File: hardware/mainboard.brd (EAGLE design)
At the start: 160 x 100 mm, 88 parts, among them IC1 ATMEGA328, IC10 HM628512A_DIL32, IC11 HM628512A_DIL32, IC12 7805TV, IC13 DS1210-8PDIP, IC14 6N138, IC3 TLC074, IC4 74HCT04N, IC5 74HC238N, IC6 74HCT573N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

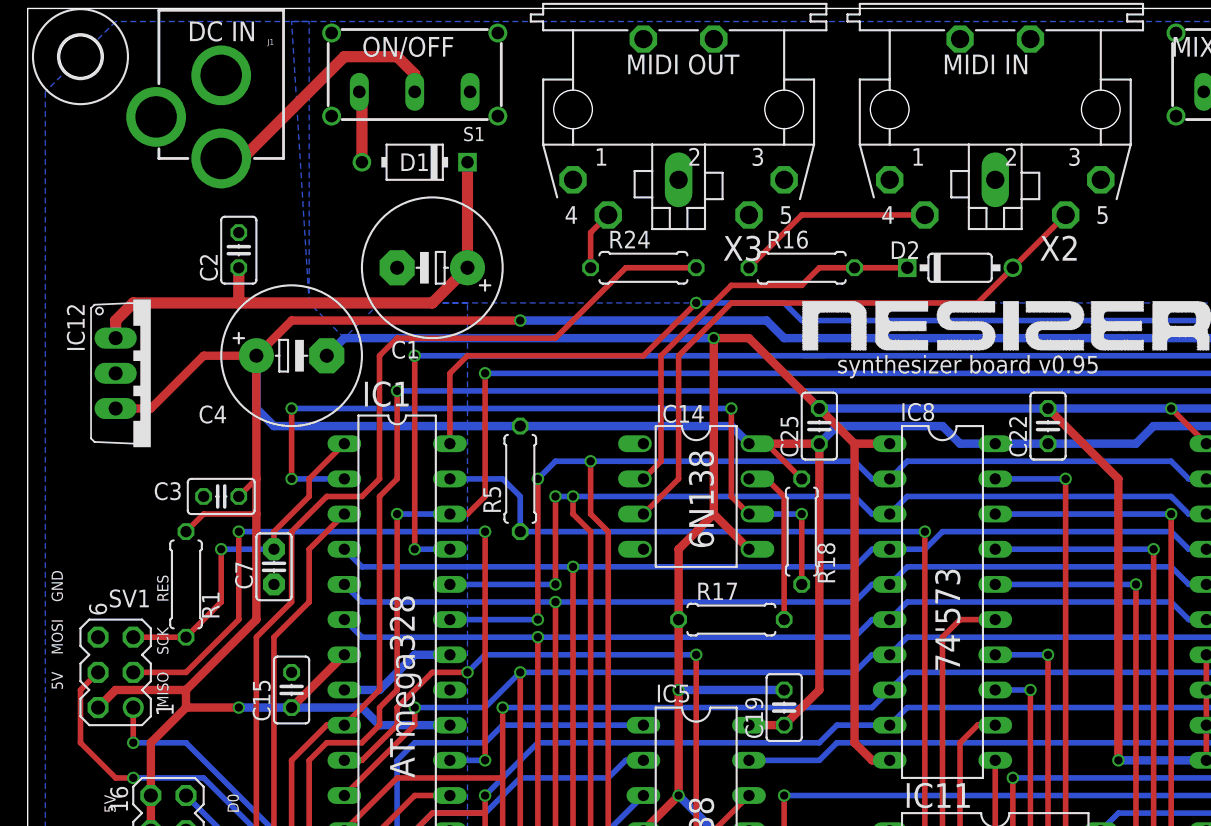
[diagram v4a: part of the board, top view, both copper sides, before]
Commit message: add 220 resistor to MIDI out
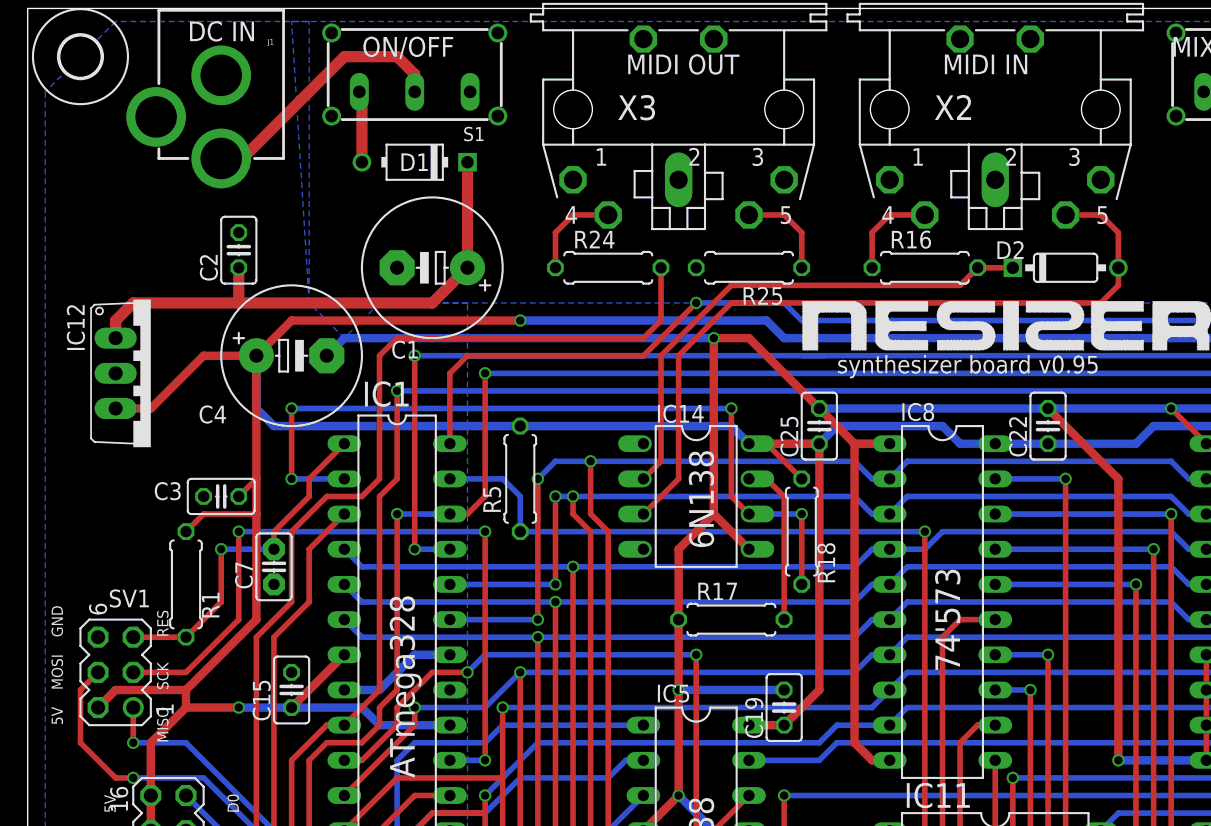
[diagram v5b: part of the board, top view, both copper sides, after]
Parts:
- added R25: 220, rcl:0207/7
- moved R16 8.89 mm to (64.8, 81.3)
- moved D2 7.62 mm to (74.9, 81.3)
- moved R24 2.54 mm to (41.9, 81.3)
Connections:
- new net N$42: R25.1, X3.5
- net GND: now also R25.2; no longer X3.5
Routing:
- net MIDI_PIN_5: track 44.6 -> 54.5 mm
- net N$34: track 29.8 -> 37.4 mm
- net MIDI_PIN_4: track 14.3 -> 6.88 mm
- net N$42: track 0.00 -> 6.88 mm
- net N$41: track 4.34 -> 6.88 mm
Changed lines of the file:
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@@
 <text x="3.81" y="26.67" size="0.8128" layer="25" font="vector" rot="R90">FRONT PANEL CONNECTOR</text>
 <text x="142.24" y="96.52" size="1.4224" layer="25" font="vector">VOLUME</text>
-<text x="2.54" y="50.8" size="0.8128" layer="25" font="vector" rot="R90">5V</text>
-<text x="2.54" y="57.15" size="0.8128" layer="25" font="vector" rot="R90">GND</text>
-<text x="2.54" y="53.34" size="0.8128" layer="25" font="vector" rot="R90">MOSI</text>
-<text x="10.16" y="49.53" size="0.8128" layer="25" font="vector" rot="R90">MISO</text>
-<text x="10.16" y="53.34" size="0.8128" layer="25" font="vector" rot="R90">SCK</text>
-<text x="10.16" y="57.15" size="0.8128" layer="25" font="vector" rot="R90">RES</text>
+<text x="2.54" y="48.26" size="0.8128" layer="25" font="vector" rot="R90">5V</text>
+<text x="2.54" y="54.61" size="0.8128" layer="25" font="vector" rot="R90">GND</text>
+<text x="2.54" y="50.8" size="0.8128" layer="25" font="vector" rot="R90">MOSI</text>
+<text x="10.16" y="46.99" size="0.8128" layer="25" font="vector" rot="R90">MISO</text>
+<text x="10.16" y="50.8" size="0.8128" layer="25" font="vector" rot="R90">SCK</text>
+<text x="10.16" y="54.61" size="0.8128" layer="25" font="vector" rot="R90">RES</text>
 <text x="71.12" y="12.7" size="1.778" layer="21" rot="R90">SRAM 512kx8</text>
 <text x="92.71" y="12.7" size="1.778" layer="21" rot="R90">SRAM 512kx8</text>
@@
 <attribute name="OC_FARNELL" value="9860150" x="48.26" y="64.77" size="1.778" layer="27" rot="R270" display="off"/>
 </element>
-<element name="R16" library="rcl" package="0207/7" value="220" x="55.88" y="81.28"/>
-<element name="D2" library="gm-diodes" package="DO35-3" value="1N914.3" x="67.31" y="81.28" smashed="yes">
-<attribute name="NAME" x="62.23" y="81.915" size="1.27" layer="25" ratio="12"/>
-<attribute name="VALUE" x="65.024" y="78.613" size="1.27" layer="27" ratio="12"/>
+<element name="R16" library="rcl" package="0207/7" value="220" x="64.77" y="81.28"/>
+<element name="D2" library="gm-diodes" package="DO35-3" value="1N914.3" x="74.93" y="81.28" smashed="yes">
+<attribute name="NAME" x="69.85" y="81.915" size="1.27" layer="25" ratio="12"/>
+<attribute name="VALUE" x="72.644" y="78.613" size="1.27" layer="27" ratio="12"/>
 </element>
 <element name="R18" library="rcl" package="0207/7" value="220" x="55.88" y="62.23" smashed="yes" rot="R90">
@@
 <attribute name="VALUE" x="143.891" y="45.974" size="1.27" layer="27" ratio="10" rot="R180"/>
 </element>
-<element name="X2" library="con-hirschmann" package="MAB5SH" value="MAB5SH" x="69.85" y="92.71" rot="R180">
+<element name="X2" library="con-hirschmann" package="MAB5SH" value="MAB5SH" x="69.85" y="92.71" smashed="yes" rot="R180">
 <attribute name="MPN" value="" x="69.85" y="92.71" size="1.778" layer="27" rot="R180" display="off"/>
 <attribute name="OC_NEWARK" value="unknown" x="69.85" y="92.71" size="1.778" layer="27" rot="R180" display="off"/>
 <attribute name="OC_FARNELL" value="809883" x="69.85" y="92.71" size="1.778" layer="27" rot="R180" display="off"/>
 <attribute name="MF" value="" x="69.85" y="92.71" size="1.778" layer="27" rot="R180" display="off"/>
+<attribute name="NAME" x="68.326" y="93.726" size="1.778" layer="25" ratio="10" rot="R180"/>
+<attribute name="VALUE" x="74.93" y="92.71" size="1.778" layer="27" ratio="10" rot="R180"/>
 </element>
 <element name="IC13" library="maxim-custom" package="DIL08" value="DS1210-8PDIP" x="121.92" y="6.35" rot="R270"/>
@@
 </element>
 <element name="C7" library="capacitor-wima" package="C2.5-2" value="10n" x="17.78" y="59.69" rot="R90"/>
-<element name="X3" library="con-hirschmann" package="MAB5SH" value="MAB5SH" x="46.99" y="92.71" rot="R180">
+<element name="X3" library="con-hirschmann" package="MAB5SH" value="MAB5SH" x="46.99" y="92.71" smashed="yes" rot="R180">
 <attribute name="OC_NEWARK" value="unknown" x="46.99" y="92.71" size="1.778" layer="27" rot="R180" display="off"/>
 <attribute name="MF" value="" x="46.99" y="92.71" size="1.778" layer="27" rot="R180" display="off"/>
 <attribute name="MPN" value="" x="46.99" y="92.71" size="1.778" layer="27" rot="R180" display="off"/>
 <attribute name="OC_FARNELL" value="809883" x="46.99" y="92.71" size="1.778" layer="27" rot="R180" display="off"/>
-</element>
-<element name="R24" library="rcl" package="0207/7" value="220" x="44.45" y="81.28"/>
+<attribute name="NAME" x="45.466" y="93.726" size="1.778" layer="25" ratio="10" rot="R180"/>
+<attribute name="VALUE" x="52.07" y="92.71" size="1.778" layer="27" ratio="10" rot="R180"/>
+</element>
+<element name="R24" library="rcl" package="0207/7" value="220" x="41.91" y="81.28"/>
+<element name="R25" library="rcl" package="0207/7" value="220" x="52.07" y="81.28" rot="R180"/>
 </elements>
 <signals>
@@
 <contactref element="C7" pad="1"/>
 <contactref element="X3" pad="2"/>
-<contactref element="X3" pad="5"/>
 <contactref element="X3" pad="PE@"/>
 <contactref element="X3" pad="PE"/>
+<contactref element="R25" pad="2"/>
 </signal>
 <signal name="VCC">
@@
 <signal name="MIDI_PIN_4">
 <contactref element="R16" pad="1"/>
-<wire x1="52.07" y1="81.28" x2="55.88" y2="85.09" width="0.4064" layer="1"/>
 <contactref element="X2" pad="4"/>
-<wire x1="64.77" y1="85.09" x2="55.88" y2="85.09" width="0.4064" layer="1"/>
+<wire x1="60.96" y1="81.28" x2="60.96" y2="83.82" width="0.4064" layer="1"/>
+<wire x1="60.96" y1="83.82" x2="62.23" y2="85.09" width="0.4064" layer="1"/>
+<wire x1="62.23" y1="85.09" x2="64.77" y2="85.09" width="0.4064" layer="1"/>
 </signal>
 <signal name="MIDI_PIN_5">
@@
 <contactref element="D2" pad="A"/>
 <wire x1="44.45" y1="63.5" x2="46.99" y2="66.04" width="0.4064" layer="1"/>
-<wire x1="71.12" y1="81.28" x2="68.58" y2="78.74" width="0.4064" layer="1"/>
-<wire x1="68.58" y1="78.74" x2="50.8" y2="78.74" width="0.4064" layer="1"/>
+<wire x1="78.74" y1="81.28" x2="78.74" y2="80.01" width="0.4064" layer="1"/>
+<wire x1="78.74" y1="80.01" x2="77.47" y2="78.74" width="0.4064" layer="1"/>
+<wire x1="77.47" y1="78.74" x2="50.8" y2="78.74" width="0.4064" layer="1"/>
 <wire x1="50.8" y1="78.74" x2="46.99" y2="74.93" width="0.4064" layer="1"/>
 <wire x1="46.99" y1="74.93" x2="46.99" y2="66.04" width="0.4064" layer="1"/>
 <contactref element="X2" pad="5"/>
-<wire x1="74.93" y1="85.09" x2="71.12" y2="81.28" width="0.4064" layer="1"/>
+<wire x1="74.93" y1="85.09" x2="77.47" y2="85.09" width="0.4064" layer="1"/>
+<wire x1="77.47" y1="85.09" x2="78.74" y2="83.82" width="0.4064" layer="1"/>
+<wire x1="78.74" y1="83.82" x2="78.74" y2="81.28" width="0.4064" layer="1"/>
 </signal>
 <signal name="N$34">
@@
 <wire x1="45.72" y1="74.93" x2="45.72" y2="67.31" width="0.4064" layer="1"/>
 <wire x1="45.72" y1="67.31" x2="44.45" y2="66.04" width="0.4064" layer="1"/>
-<wire x1="63.5" y1="81.28" x2="59.69" y2="81.28" width="0.4064" layer="1"/>
-<wire x1="59.69" y1="81.28" x2="57.15" y2="81.28" width="0.4064" layer="1"/>
-<wire x1="57.15" y1="81.28" x2="55.88" y2="80.01" width="0.4064" layer="1"/>
-<wire x1="55.88" y1="80.01" x2="50.8" y2="80.01" width="0.4064" layer="1"/>
+<wire x1="71.12" y1="81.28" x2="68.58" y2="81.28" width="0.4064" layer="1"/>
+<wire x1="67.31" y1="80.01" x2="50.8" y2="80.01" width="0.4064" layer="1"/>
 <wire x1="50.8" y1="80.01" x2="45.72" y2="74.93" width="0.4064" layer="1"/>
+<wire x1="67.31" y1="80.01" x2="68.58" y2="81.28" width="0.4064" layer="1"/>
 </signal>
 <signal name="N$35">
@@
 <contactref element="IC4" pad="12"/>
 <contactref element="R24" pad="2"/>
-<wire x1="48.26" y1="81.28" x2="43.18" y2="81.28" width="0.4064" layer="1"/>
-<wire x1="43.18" y1="81.28" x2="38.1" y2="76.2" width="0.4064" layer="1"/>
-<wire x1="38.1" y1="76.2" x2="26.67" y2="76.2" width="0.4064" layer="1"/>
+<wire x1="45.72" y1="81.28" x2="45.72" y2="77.47" width="0.4064" layer="1"/>
+<wire x1="45.72" y1="77.47" x2="44.45" y2="76.2" width="0.4064" layer="1"/>
+<wire x1="44.45" y1="76.2" x2="26.67" y2="76.2" width="0.4064" layer="1"/>
 <wire x1="26.67" y1="76.2" x2="25.4" y2="74.93" width="0.4064" layer="1"/>
 <wire x1="25.4" y1="74.93" x2="25.4" y2="66.04" width="0.4064" layer="1"/>
@@
 <contactref element="R24" pad="1"/>
 <contactref element="X3" pad="4"/>
-<wire x1="40.64" y1="81.28" x2="40.64" y2="83.82" width="0.4064" layer="1"/>
-<wire x1="40.64" y1="83.82" x2="41.91" y2="85.09" width="0.4064" layer="1"/>
+<wire x1="38.1" y1="81.28" x2="38.1" y2="83.82" width="0.4064" layer="1"/>
+<wire x1="38.1" y1="83.82" x2="39.37" y2="85.09" width="0.4064" layer="1"/>
+<wire x1="39.37" y1="85.09" x2="41.91" y2="85.09" width="0.4064" layer="1"/>
+</signal>
+<signal name="N$42">
+<contactref element="X3" pad="5"/>
+<contactref element="R25" pad="1"/>
+<wire x1="52.07" y1="85.09" x2="54.61" y2="85.09" width="0.4064" layer="1"/>
+<wire x1="54.61" y1="85.09" x2="55.88" y2="83.82" width="0.4064" layer="1"/>
+<wire x1="55.88" y1="83.82" x2="55.88" y2="81.28" width="0.4064" layer="1"/>
 </signal>
 </signals>
